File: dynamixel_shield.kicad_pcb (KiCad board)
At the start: 2 copper layers, 68.6 x 53.3 mm, 27 parts, among them P1 BARREL_JACK, P2 CONN_01X02, P3 CONN_01X03, P4 CONN_01X03, P5 CONN_01X03, P6 CONN_01X03, P7 CONN_01X03, P8 CONN_01X03, P9 CONN_01X03, Q1 MOSFET_N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

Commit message: add small traces to vias, so that they are not disconnected when you refill the ground zones
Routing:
- net GND: track 2.09 -> 20.9 mm
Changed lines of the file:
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@@
     (thickness 1.6)
     (drawings 19)
-    (tracks 209)
+    (tracks 219)
     (zones 0)
     (modules 27)
@@
   (segment (start 110.744 99.06) (end 105.664 104.14) (width 1.5) (layer F.Cu) (net 10))
   (segment (start 105.664 104.14) (end 105.664 104.648) (width 1.5) (layer F.Cu) (net 10))
+  (segment (start 80.137 99.949) (end 81.915 99.949) (width 0.25) (layer F.Cu) (net 11))
+  (segment (start 81.915 99.949) (end 83.439 99.949) (width 0.25) (layer B.Cu) (net 11))
+  (via (at 81.915 99.949) (size 0.6) (drill 0.4) (layers F.Cu B.Cu) (net 11))
+  (segment (start 102.87 73.533) (end 102.87 75.565) (width 0.25) (layer B.Cu) (net 11))
+  (segment (start 102.87 75.565) (end 102.87 77.343) (width 0.25) (layer F.Cu) (net 11))
   (via (at 102.87 75.565) (size 0.6) (drill 0.4) (layers F.Cu B.Cu) (net 11))
+  (segment (start 105.029 89.789) (end 105.029 91.313) (width 0.25) (layer F.Cu) (net 11))
+  (segment (start 105.029 91.313) (end 105.029 92.837) (width 0.25) (layer B.Cu) (net 11))
   (via (at 105.029 91.313) (size 0.6) (drill 0.4) (layers F.Cu B.Cu) (net 11))
-  (via (at 81.915 99.949) (size 0.6) (drill 0.4) (layers F.Cu B.Cu) (net 11))
+  (segment (start 88.138 79.756) (end 88.138 81.661) (width 0.25) (layer B.Cu) (net 11))
+  (segment (start 88.138 81.661) (end 88.138 83.439) (width 0.25) (layer F.Cu) (net 11))
   (via (at 88.138 81.661) (size 0.6) (drill 0.4) (layers F.Cu B.Cu) (net 11))
+  (segment (start 76.708 70.358) (end 79.121 70.358) (width 0.25) (layer F.Cu) (net 11))
+  (segment (start 79.121 70.358) (end 81.661 70.358) (width 0.25) (layer B.Cu) (net 11))
   (via (at 79.121 70.358) (size 0.6) (drill 0.4) (layers F.Cu B.Cu) (net 11))
   (segment (start 87.63 65.151) (end 89.535 65.024) (width 0.25) (layer F.Cu) (net 11))

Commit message: remove vias in ground plane
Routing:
- net GND: track 20.9 -> 2.09 mm, vias 6 -> 1
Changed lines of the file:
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@@
     (thickness 1.6)
     (drawings 19)
-    (tracks 219)
+    (tracks 204)
     (zones 0)
     (modules 27)
@@
   (segment (start 110.744 99.06) (end 105.664 104.14) (width 1.5) (layer F.Cu) (net 10))
   (segment (start 105.664 104.14) (end 105.664 104.648) (width 1.5) (layer F.Cu) (net 10))
-  (segment (start 80.137 99.949) (end 81.915 99.949) (width 0.25) (layer F.Cu) (net 11))
-  (segment (start 81.915 99.949) (end 83.439 99.949) (width 0.25) (layer B.Cu) (net 11))
-  (via (at 81.915 99.949) (size 0.6) (drill 0.4) (layers F.Cu B.Cu) (net 11))
-  (segment (start 102.87 73.533) (end 102.87 75.565) (width 0.25) (layer B.Cu) (net 11))
-  (segment (start 102.87 75.565) (end 102.87 77.343) (width 0.25) (layer F.Cu) (net 11))
-  (via (at 102.87 75.565) (size 0.6) (drill 0.4) (layers F.Cu B.Cu) (net 11))
-  (segment (start 105.029 89.789) (end 105.029 91.313) (width 0.25) (layer F.Cu) (net 11))
-  (segment (start 105.029 91.313) (end 105.029 92.837) (width 0.25) (layer B.Cu) (net 11))
-  (via (at 105.029 91.313) (size 0.6) (drill 0.4) (layers F.Cu B.Cu) (net 11))
-  (segment (start 88.138 79.756) (end 88.138 81.661) (width 0.25) (layer B.Cu) (net 11))
-  (segment (start 88.138 81.661) (end 88.138 83.439) (width 0.25) (layer F.Cu) (net 11))
-  (via (at 88.138 81.661) (size 0.6) (drill 0.4) (layers F.Cu B.Cu) (net 11))
-  (segment (start 76.708 70.358) (end 79.121 70.358) (width 0.25) (layer F.Cu) (net 11))
-  (segment (start 79.121 70.358) (end 81.661 70.358) (width 0.25) (layer B.Cu) (net 11))
-  (via (at 79.121 70.358) (size 0.6) (drill 0.4) (layers F.Cu B.Cu) (net 11))
   (segment (start 87.63 65.151) (end 89.535 65.024) (width 0.25) (layer F.Cu) (net 11))
   (via (at 89.662 64.897) (size 0.6) (drill 0.4) (layers F.Cu B.Cu) (net 11))

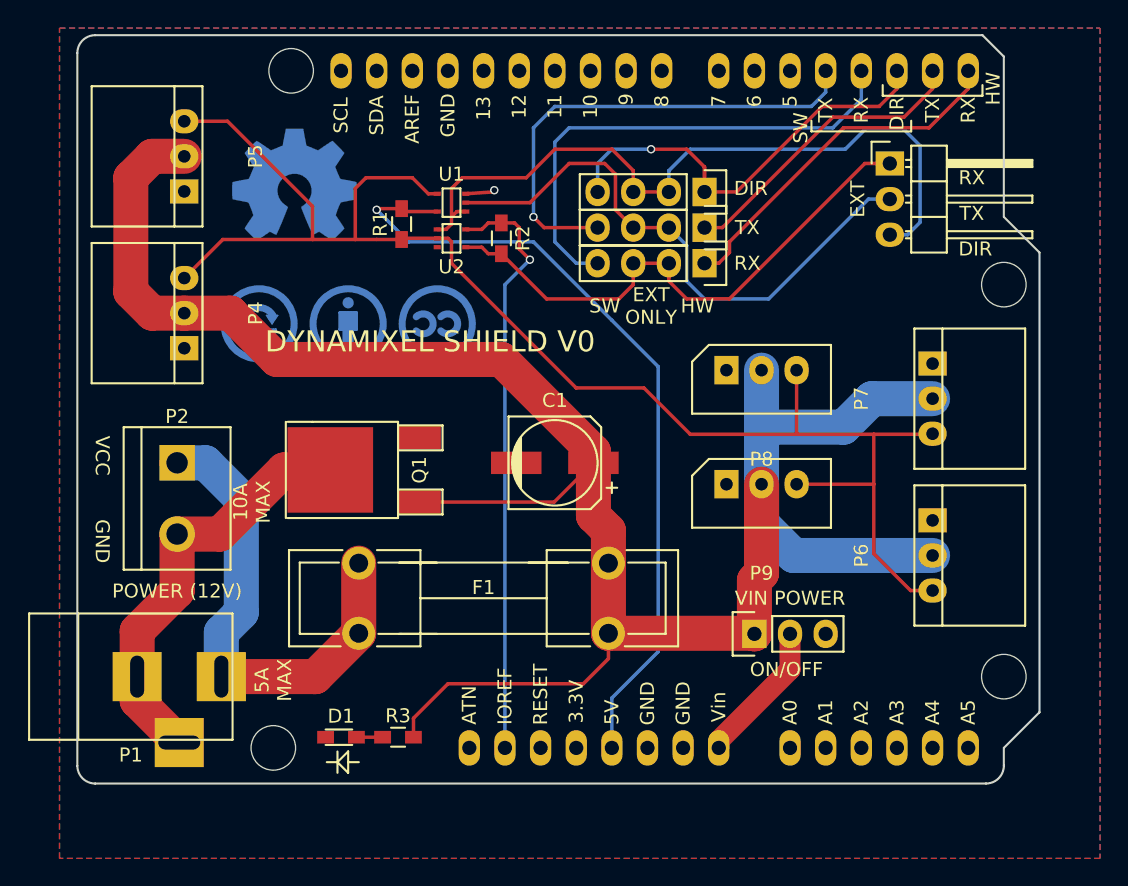
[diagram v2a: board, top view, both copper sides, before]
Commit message: update pcb with new resistors
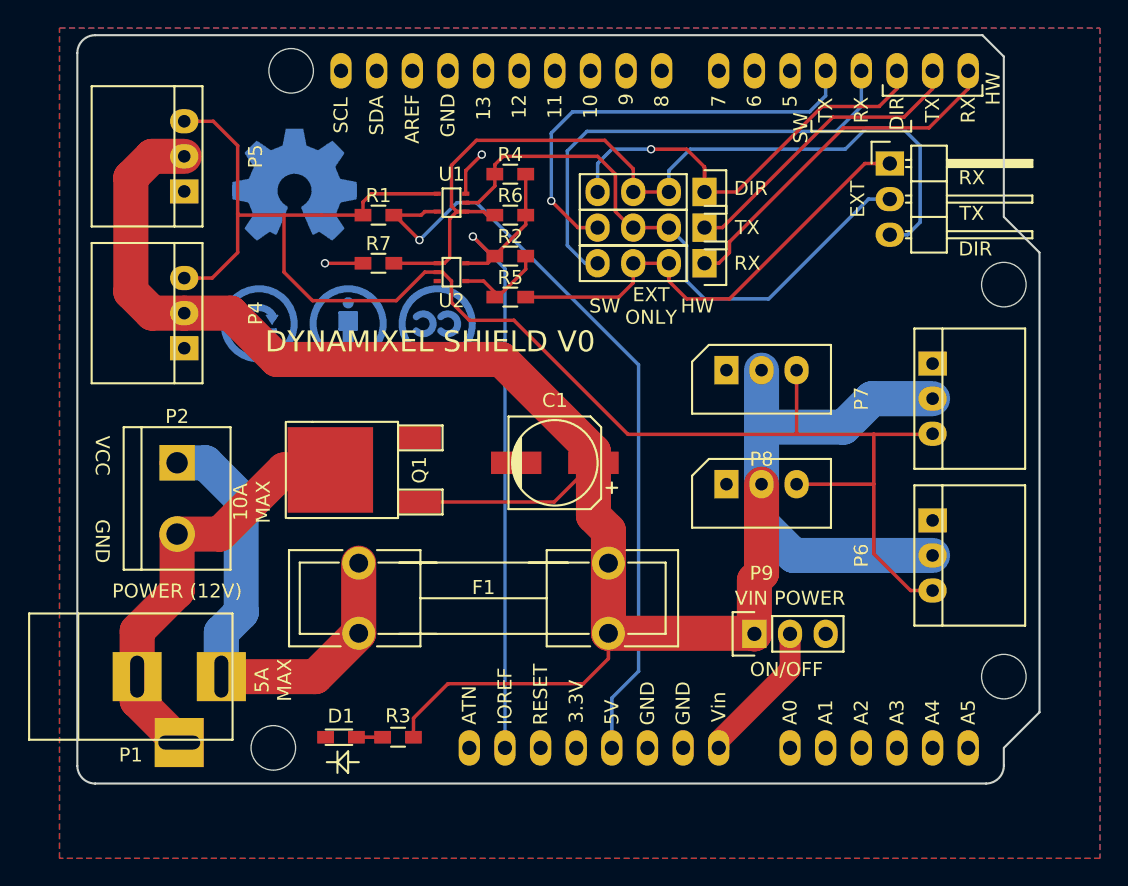
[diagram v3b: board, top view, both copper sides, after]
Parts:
- added R4: 10K, Resistors_SMD:R_0603_HandSoldering, F.Cu at (90.8, 63.8)
- added R5: 500, Resistors_SMD:R_0603_HandSoldering, F.Cu at (90.8, 72.5)
- added R6: 10K, Resistors_SMD:R_0603_HandSoldering, F.Cu at (90.8, 66.7)
- added R7: 10K, Resistors_SMD:R_0603_HandSoldering, F.Cu at (81.4, 70.1)
- moved U2 2.41 mm to (86.6, 70.7)
- moved R1 1.77 mm to (81.4, 66.7), turned to 180 degrees
- moved R2 1.42 mm to (90.8, 69.6), turned to 0 degrees
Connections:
- R2 pad 2: /RXD -> Net-(R2-Pad2)
- U2 pad 4: /RXD -> Net-(R2-Pad2)
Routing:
- net /DIRECTION_PORT: track 53.4 -> 63.0 mm
- net Net-(R2-Pad2): track 0.00 -> 6.70 mm
- net /IOREF: track 42.3 -> 48.6 mm
- net /RXD: track 40.5 -> 34.6 mm
- net /DATA: track 109.5 -> 113.8 mm
- net GND: track 2.09 -> 5.98 mm, vias 1 -> 2
- net /SW_TXD: track 34.6 -> 31.4 mm
- net /SW_RXD: track 35.9 -> 34.2 mm
- net /TXD: track 41.6 -> 42.9 mm
- net +5V: track 57.7 -> 56.5 mm
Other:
- rule pad_to_mask_clearance: 0.2 -> 0.13
